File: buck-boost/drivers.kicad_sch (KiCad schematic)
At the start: 10 parts, among them U4 TBA1-1212E, U5 TBA1-1212E

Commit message: Added load switch and relay drivers
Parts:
- added D13, D16: D_Small_Filled, Diode_SMD:D_SOD-123, symbol Device:D_Small_Filled
- added D14, D15: LED_Small_Filled, symbol Device:LED_Small_Filled
- added JP1: Jumper_2_Bridged, TestPoint:TestPoint_2Pads_Pitch2.54mm_Drill0.8mm, symbol Jumper:Jumper_2_Bridged
- added Q6, Q7, Q8, Q9: Q_NPN_BEC, Package_TO_SOT_SMD:SOT-23W_Handsoldering, symbol Device:Q_NPN_BEC
- added R26, R27, R30, R31, R34: 100k, Resistor_SMD:R_0805_2012Metric_Pad1.20x1.40mm_HandSolder, symbol Device:R_Small
- added R28, R32, R33, R35, R36: 1k, Resistor_SMD:R_0805_2012Metric_Pad1.20x1.40mm_HandSolder, symbol Device:R_Small
- added R29: 47R, Resistor_SMD:R_0805_2012Metric_Pad1.20x1.40mm_HandSolder, symbol Device:R_Small
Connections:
- net GND: now also Q6.2 (E), Q7.2 (E), Q8.2 (E), Q9.2 (E), R30.2, R31.2, R34.2
- net Vdd: no longer C24.1, C27.1, L2.1, L4.1
- net Vdd_S1 renamed Vcc_S1
- net Vdd_S3 renamed Vcc_S3
- new net: JP1.1 (A), R27.1, R28.1
- new net: Q6.1 (B), R26.2
- new net: Q9.1 (B), R35.2
- new net: D15.1 (K), R36.1
- new net: Q6.3 (C), Q7.1 (B), R27.2
- new net: Q7.3 (C), R28.2, R29.1
- new net: D14.1 (K), R33.1
- new net: Q8.1 (B), R32.2
- new net G_Sload: R29.2
- new net K_in: R31.1, R32.1
- new net K_in_A1: C24.1, C27.1, D13.1 (K), D14.2 (A), D15.2 (A), D16.1 (K), JP1.2 (B), L2.1, L4.1
- new net K_in_A2: D13.2 (A), Q8.3 (C), R33.2
- new net K_out: R34.1, R35.1
- new net K_out_A2: D16.2 (A), Q9.3 (C), R36.2
- new net Sload: R26.1, R30.1
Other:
- note added: "Gate drivers - S1, S2, S3, S4"
- note added: "Gate drivers - Sload"
- note added: "Notes [1] Connecting S2 to IN- of the high-side driver and S1 to IN- of the low-side driver prevents that both MOSFETs are turned on at the same time. [2] It wouldn't be necessary to use an isolated gate driver for the low-side MOSFETs. However, one is used anyways due to the driver's Miller clamp functionality. Moreover, we have a single chip for all drivers, simplifying the BOM. [3] This driver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"
- note added: "Relay drivers"
- note added: "[2]"
- note added: "[3]"
- note removed: "Notes [1] Connecting S2 to IN- of the high-side driver and S1 to IN- of the low-side driver prevents that both MOSFETs are turned on at the same time."
- moved on the sheet: C24, C25, C26, C27, C28, C29, L2, L4, U4, U5

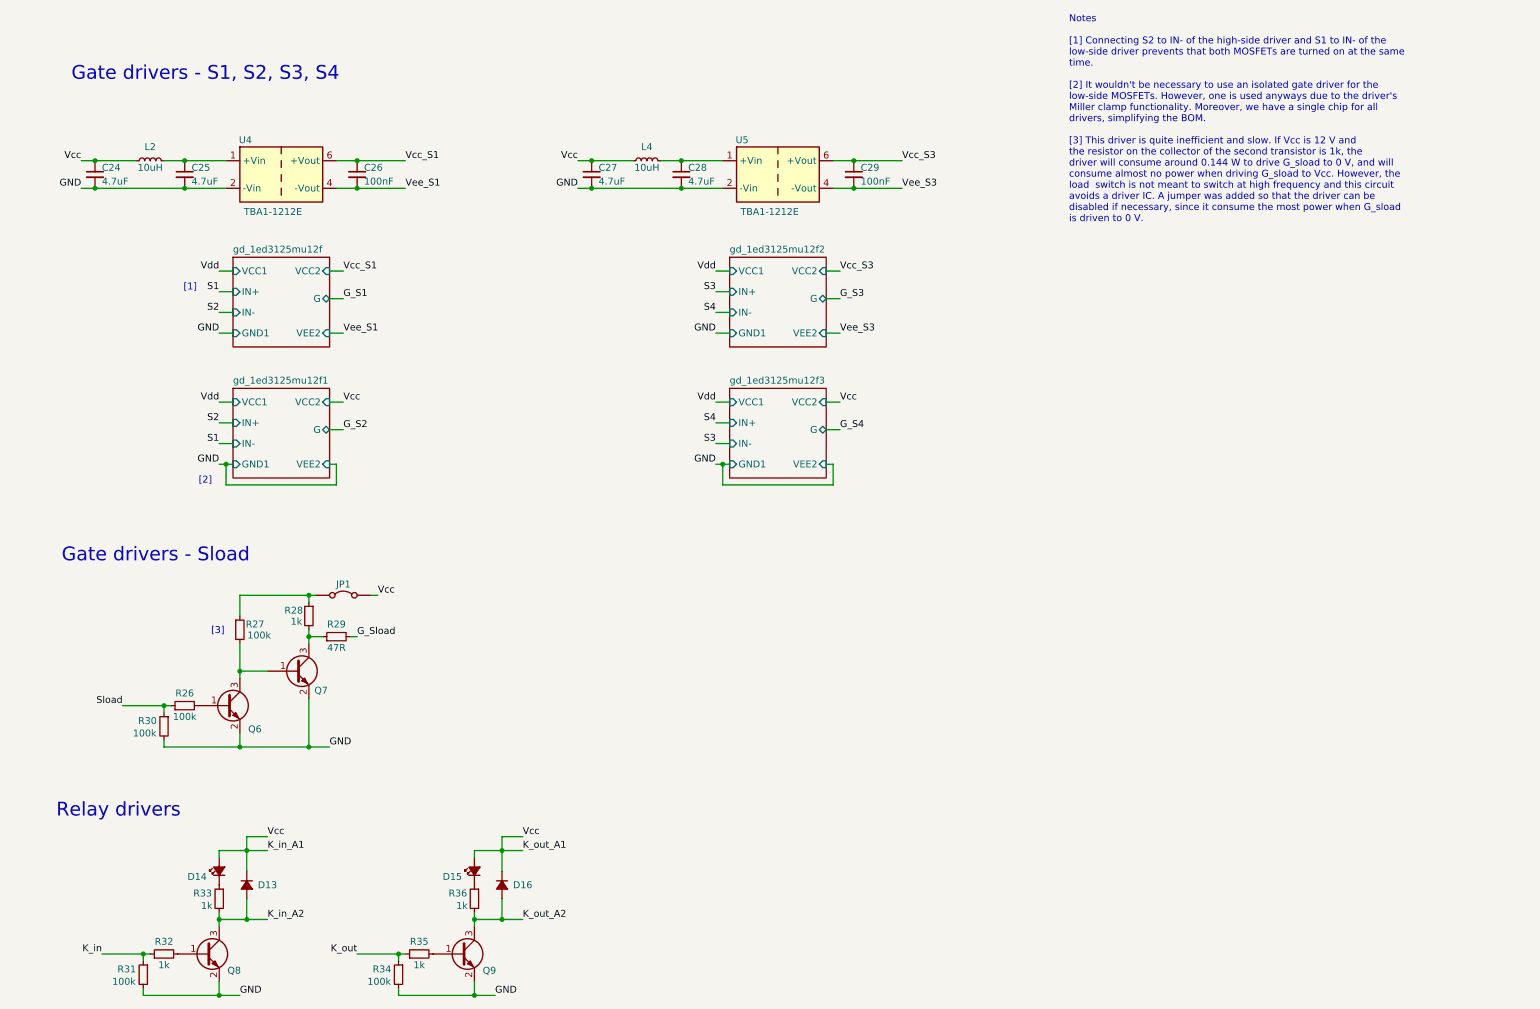
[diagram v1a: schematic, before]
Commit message: Adding connectors, test points to gate drivers
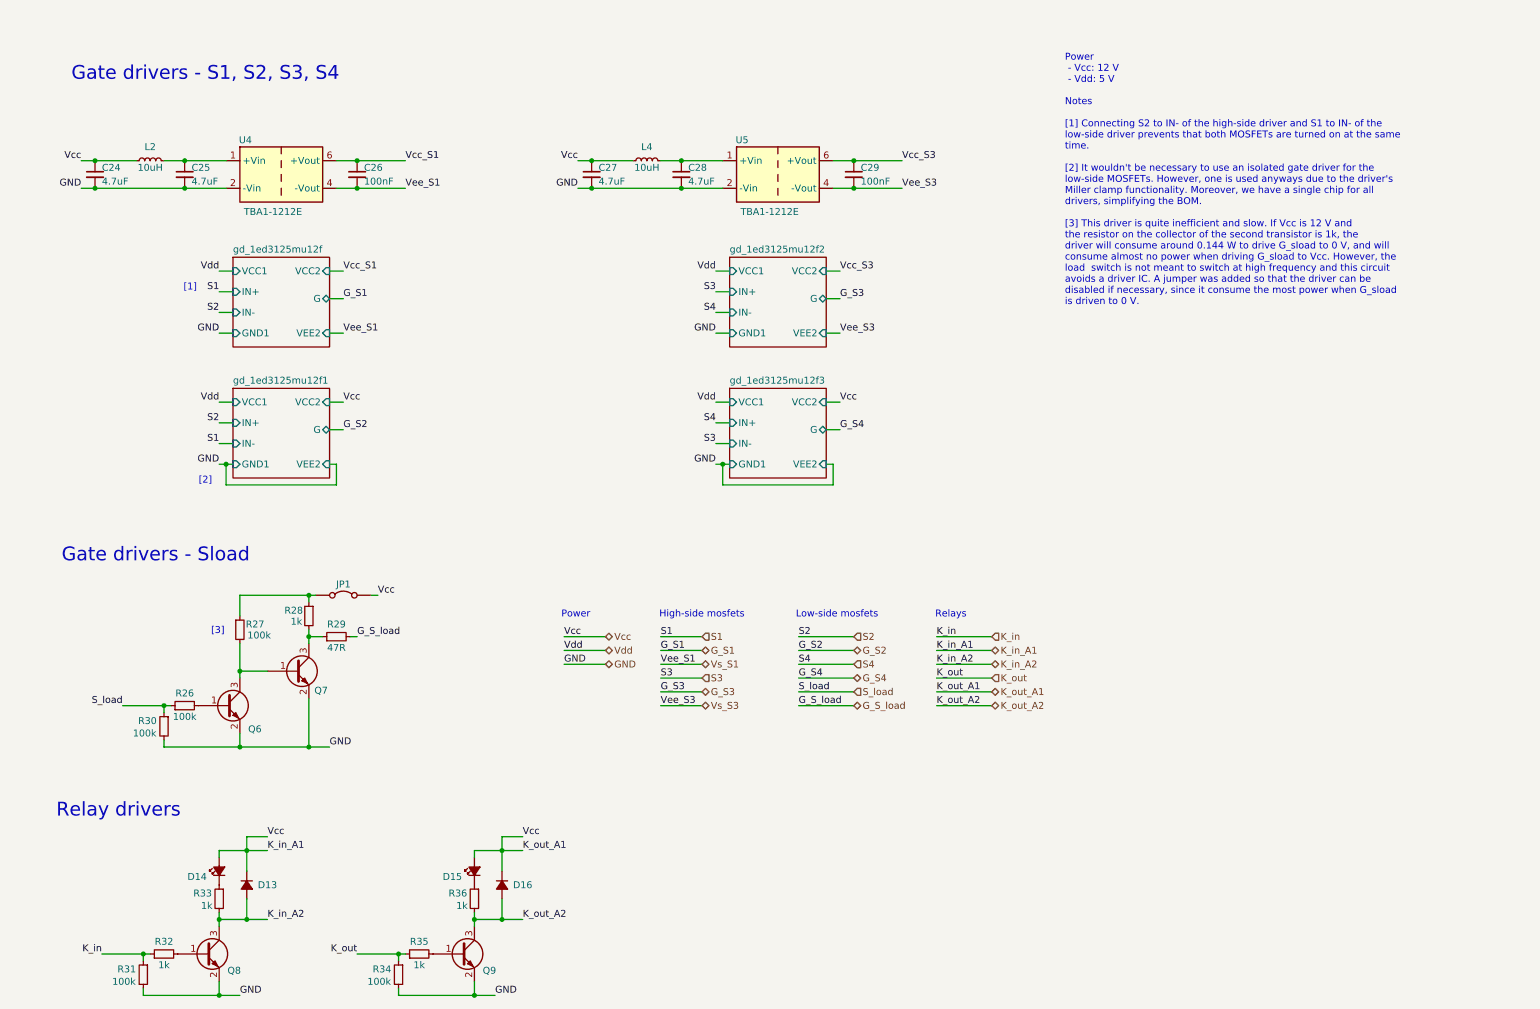
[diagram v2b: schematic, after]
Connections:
- net G_Sload renamed G_S_load
- net Sload renamed S_load
- net Vee_S1 renamed Vs_S1
- net Vee_S3 renamed Vs_S3
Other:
- note added: "High-side mosfets"
- note added: "Low-side mosfets"
- note added: "Power"
- note added: "Power - Vcc: 12 V - Vdd: 5 V Notes [1] Connecting S2 to IN- of the high-side driver and S1 to IN- of the low-side driver prevents that both MOSFETs are turned on at the same time. [2] It wouldn't be necessary to use an isolated gate driver for the low-side MOSFETs. However, one is used anyways due to the driver's Miller clamp functionality. Moreover, we have a single chip for all drivers, simplif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"
- note added: "Relays"
- note removed: "Notes [1] Connecting S2 to IN- of the high-side driver and S1 to IN- of the low-side driver prevents that both MOSFETs are turned on at the same time. [2] It wouldn't be necessary to use an isolated gate driver for the low-side MOSFETs. However, one is used anyways due to the driver's Miller clamp functionality. Moreover, we have a single chip for all drivers, simplifying the BOM. [3] This driver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"

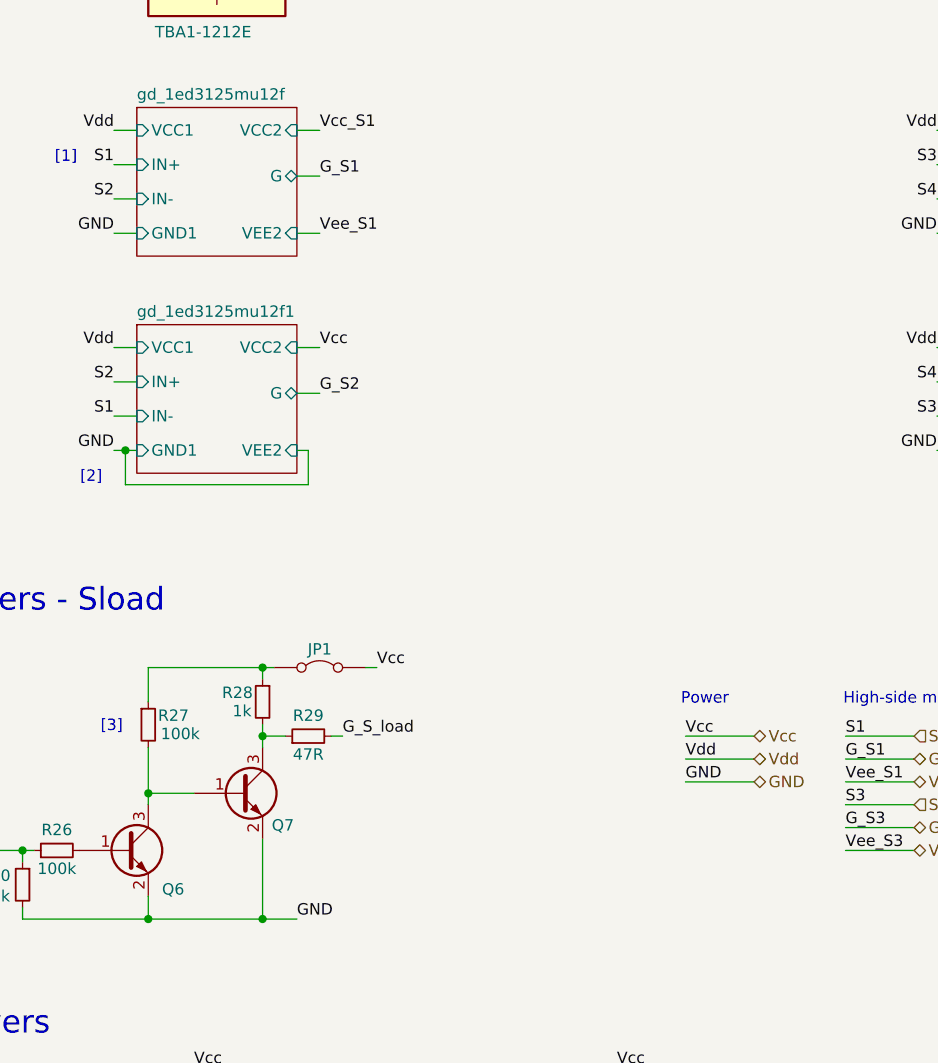
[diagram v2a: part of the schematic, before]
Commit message: Adding current and voltage measurements blocks
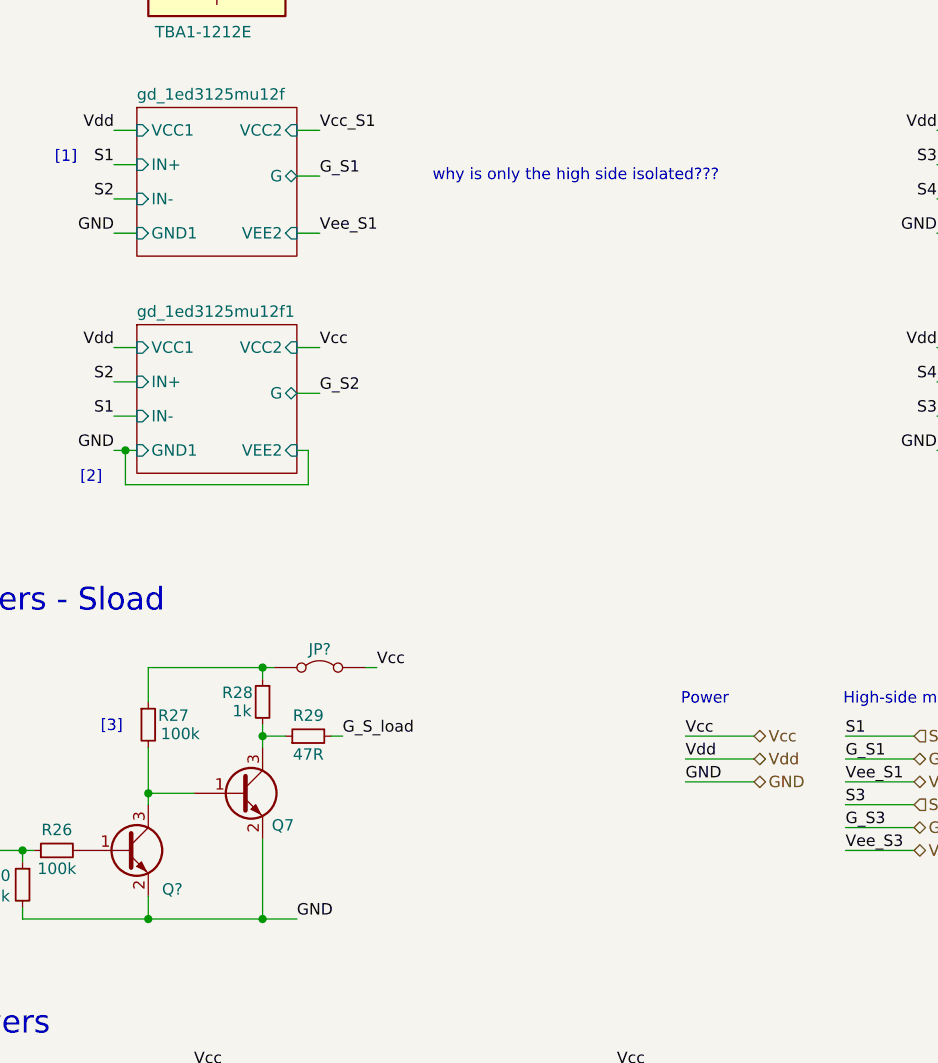
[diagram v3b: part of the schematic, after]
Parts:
- renumbered JP1 to JP?, Q6 to Q?
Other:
- note added: "why is only the high side isolated???"

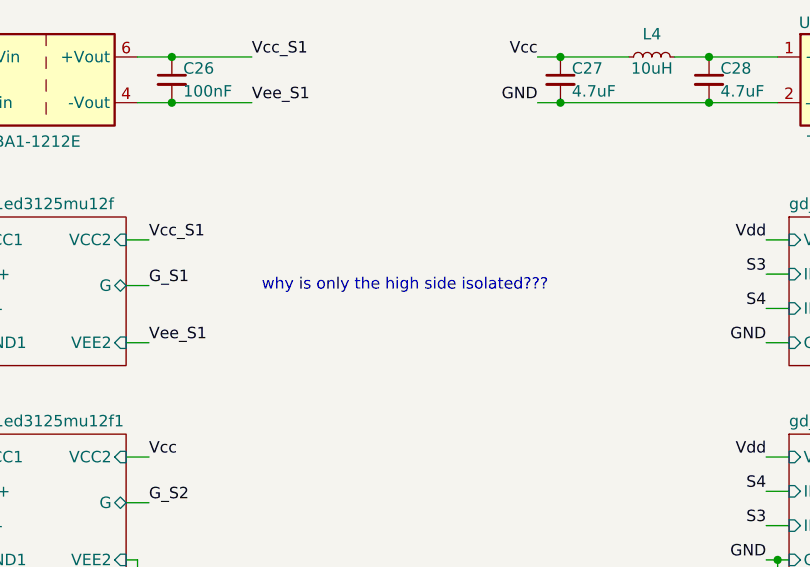
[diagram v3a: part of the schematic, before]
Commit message: Adding supply block
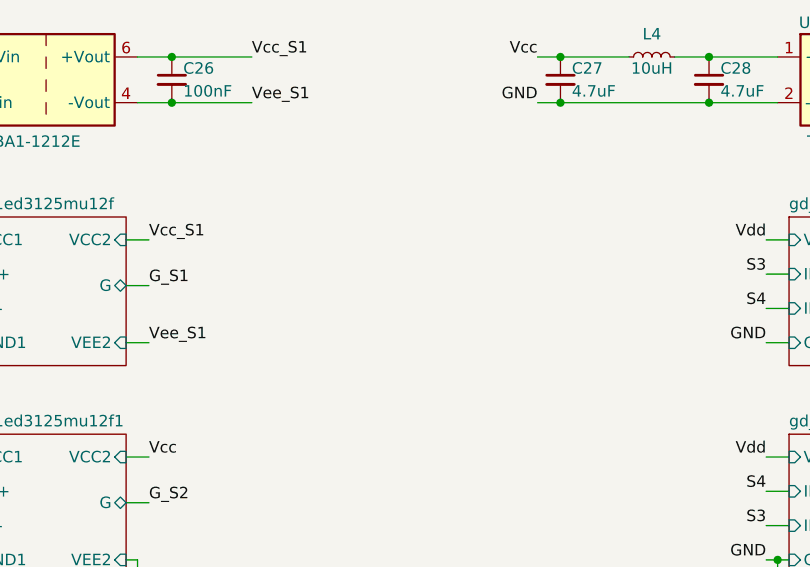
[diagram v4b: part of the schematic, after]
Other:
- note removed: "why is only the high side isolated???"
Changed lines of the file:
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@@
-		)
-	)
-	(text "why is only the high side isolated???"
-		(exclude_from_sim no)
-		(at 97.028 59.69 0)
-		(effects
-			(font
-				(size 1.27 1.27)
-			)
 		)
 	)
